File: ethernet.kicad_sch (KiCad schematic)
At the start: 44 parts, among them J5 Bus_RJ45_5-2337992-8, Q12 PJE138K, U10 ULS-12/5-D48N-C, U8 TPS2372-3RGWR, U9 ACPL-217-500E

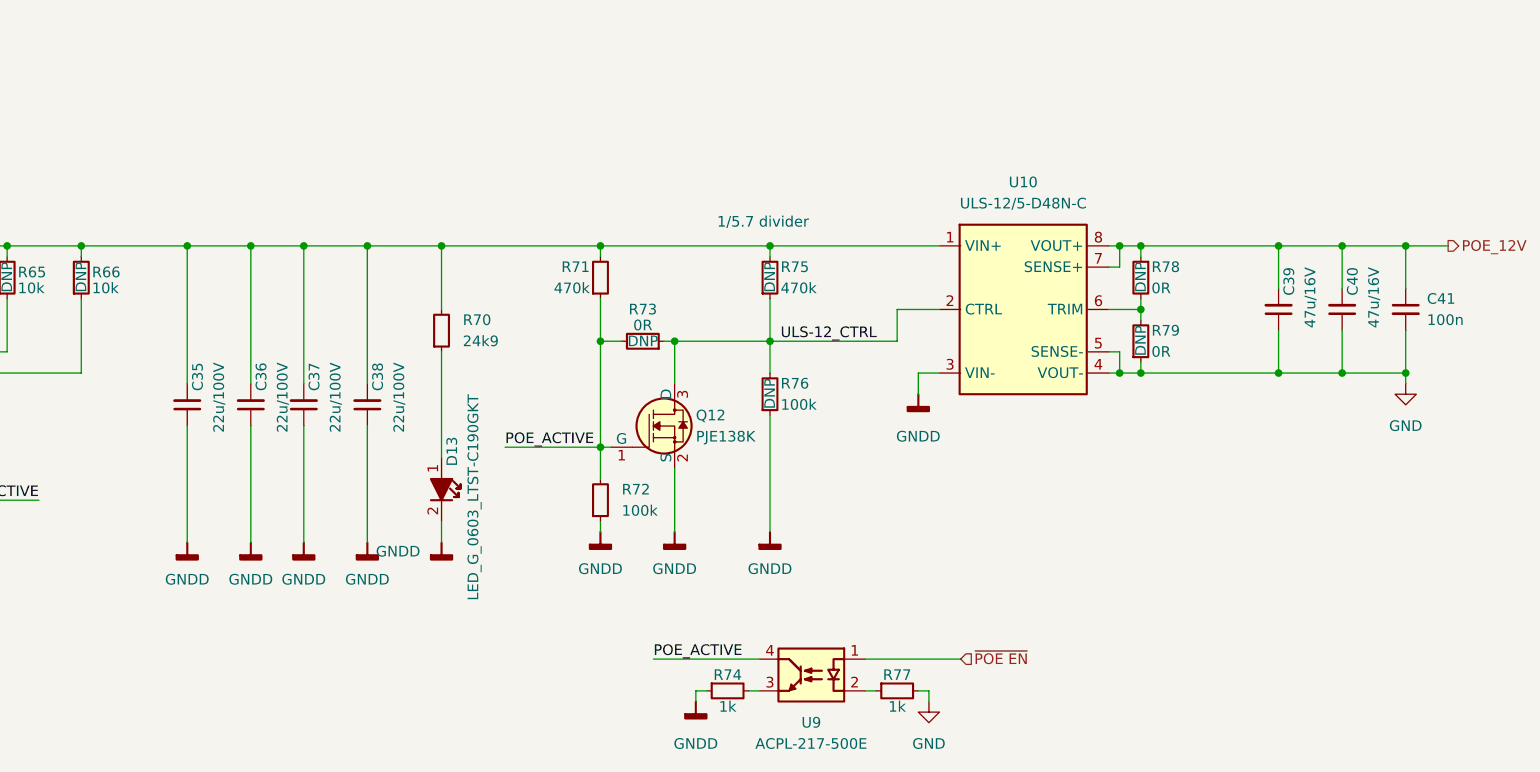
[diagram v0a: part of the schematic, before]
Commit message: [#53805] Change designators orientation in ETH sch
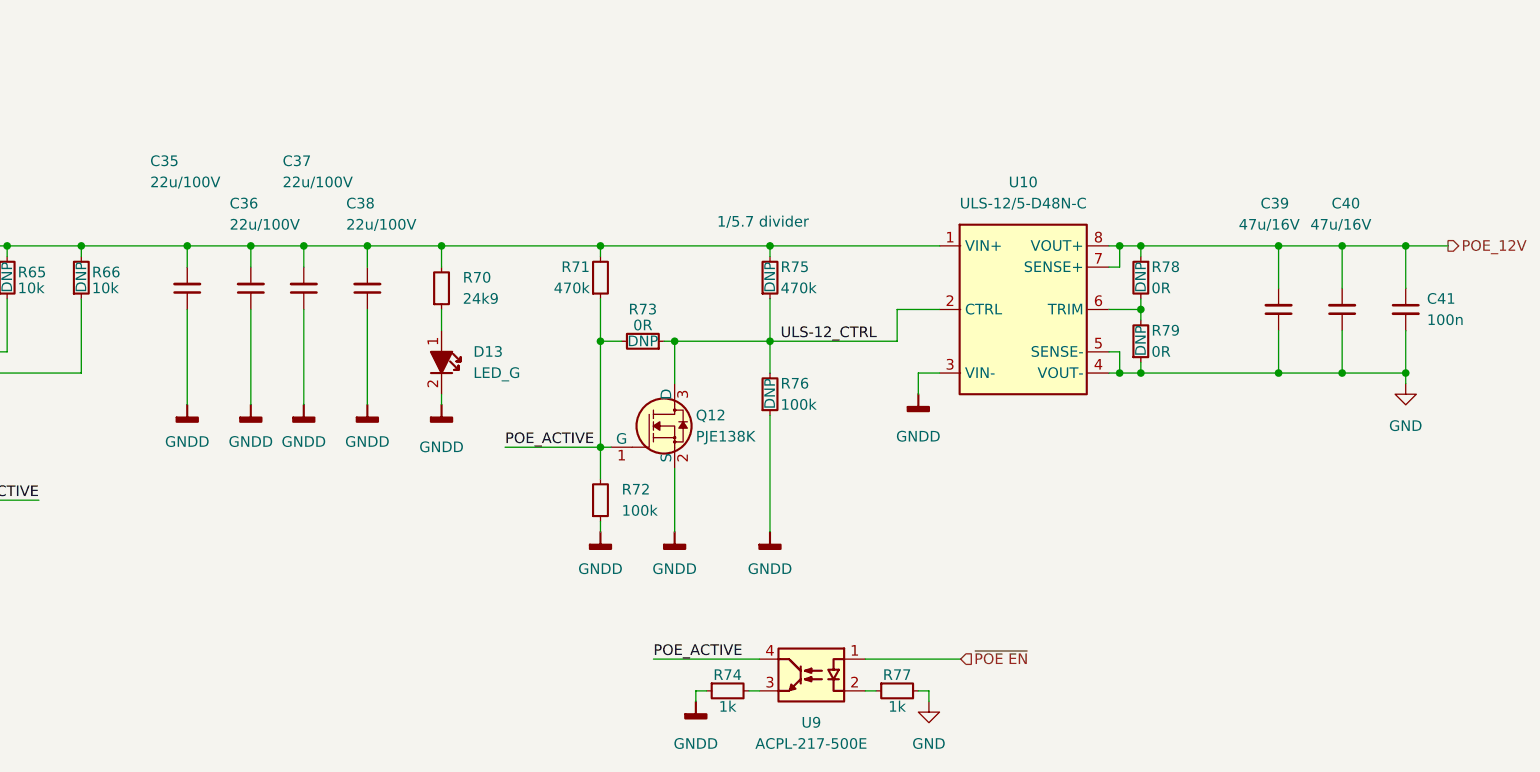
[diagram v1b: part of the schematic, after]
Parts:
- D13: value LED_G_0603_LTST-C190GKT -> LED_G
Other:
- moved on the sheet: C35, C36, C37, C38, D13, R70

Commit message: [#53901] Update capacitor symbols from lib
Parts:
- C32: Dielectric (none) -> X7R; Val 100n/100V -> 100n; Voltage (none) -> 100V
- C35, C36, C37, C38: Dielectric (none) -> X7S; Val 22u/100V -> 22u; Voltage (none) -> 100V
- C39, C40: Dielectric (none) -> X5R; Val 47u/16V -> 47u; Voltage (none) -> 16V
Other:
- moved on the sheet: C35, C36, C37, C38

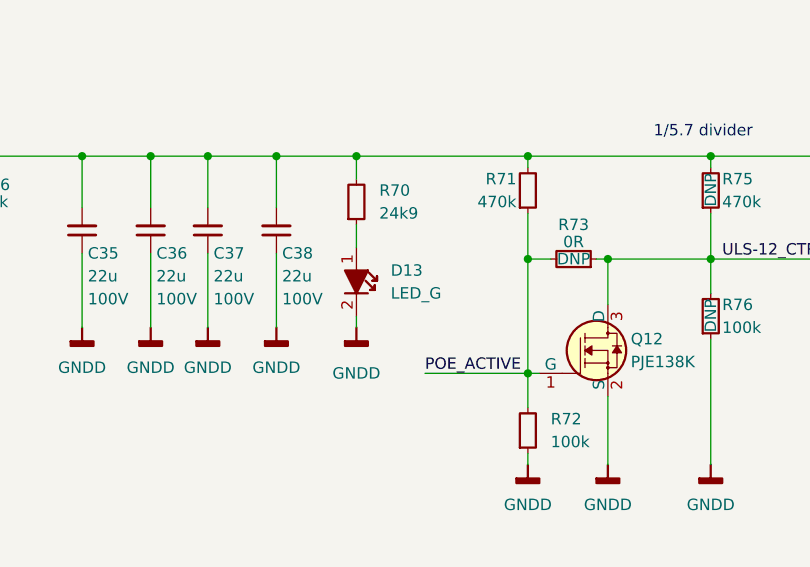
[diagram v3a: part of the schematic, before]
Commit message: [#54617] Uniform diodes MPN
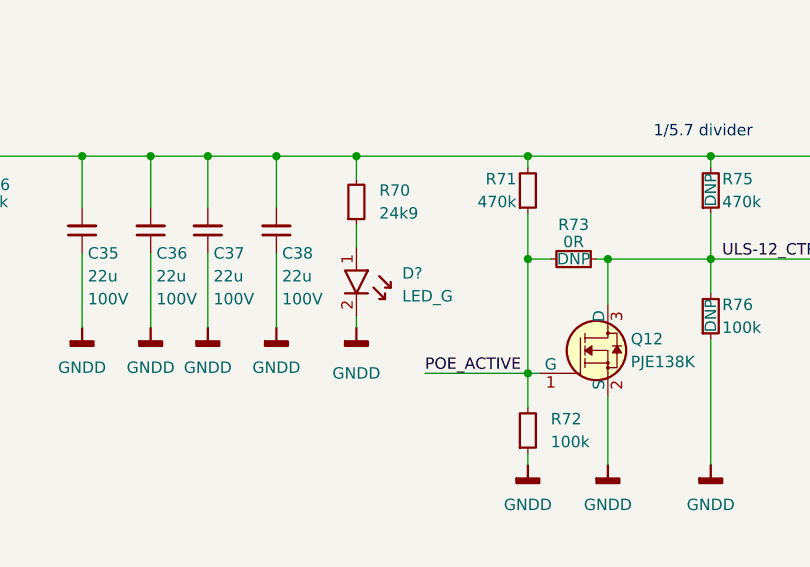
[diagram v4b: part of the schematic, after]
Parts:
- removed D13: LED_G, antmicro-footprints:LED_0603_1608Metric_G, symbol antmicroLEDIndicationDiscrete:LED_G_0603_LTST-C190GKT
- added D?: LED_G, antmicro-footprints:LED_0603_1608Metric_R, symbol antmicroLEDIndicationDiscrete:LED_R_0603_598-8D80-107F
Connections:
- net GNDD: now also D?.2
- net at R70.1: now also D?.1
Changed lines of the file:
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@@
-    (pin "2")
-  )
-  (symbol (lib_id "antmicroLEDIndicationDiscrete:LED_G_0603_LTST-C190GKT") (at 247.65 193.04 270) (unit 1)
-    (in_bom yes) (on_board yes) (fields_autoplaced)
-    (property "Reference" "D13" (id 0) (at 251.46 195.5799 90)
-      (effects (font (size 1.27 1.27)) (justify left))
-    )
-    (property "Value" "LED_G" (id 1) (at 251.46 198.1199 90)
-      (effects (font (size 1.27 1.27) (thickness 0.15)) (justify left))
-    )
-    (property "Footprint" "antmicro-footprints:LED_0603_1608Metric_G" (id 2) (at 237.49 215.9 0)
-      (effects (font (size 1.27 1.27) (thickness 0.15)) (justify left bottom) hide)
-    )
-    (property "Datasheet" "https://media.digikey.com/pdf/Data%20Sheets/Lite-On%20PDFs/LTST-C190GKT.pdf" (id 3) (at 234.95 215.9 0)
-      (effects (font (size 1.27 1.27) (thickness 0.15)) (justify left bottom) hide)
-    )
-    (property "MPN" "LTST-C190GKT" (id 4) (at 232.41 215.9 0)
-      (effects (font (size 1.27 1.27) (thickness 0.15)) (justify left bottom) hide)
-    )
-    (property "Manufacturer" "Lite-On Inc." (id 5) (at 229.87 215.9 0)
-      (effects (font (size 1.27 1.27) (thickness 0.15)) (justify left bottom) hide)
-    )
-    (property "Author" "Antmicro" (id 6) (at 227.33 215.9 0)
-      (effects (font (size 1.27 1.27) (thickness 0.15)) (justify left bottom) hide)
-    )
-    (property "License" "Apache-2.0" (id 7) (at 224.79 215.9 0)
-      (effects (font (size 1.27 1.27) (thickness 0.15)) (justify left bottom) hide)
-    )
-    (pin "1")
     (pin "2")
   )
@@
     (pin "1")
   )
+  (symbol (lib_id "antmicroLEDIndicationDiscrete:LED_R_0603_598-8D80-107F") (at 247.65 193.04 270) (unit 1)
+    (in_bom yes) (on_board yes) (fields_autoplaced)
+    (property "Reference" "D?" (id 0) (at 252.73 195.8974 90)
+      (effects (font (size 1.27 1.27) (thickness 0.15)) (justify left))
+    )
+    (property "Value" "LED_G" (id 1) (at 252.73 198.4374 90)
+      (effects (font (size 1.27 1.27) (thickness 0.15)) (justify left))
+    )
+    (property "Footprint" "antmicro-footprints:LED_0603_1608Metric_R" (id 2) (at 240.03 215.9 0)
+      (effects (font (size 1.27 1.27) (thickness 0.15)) (justify left bottom) hide)
+    )
+    (property "Datasheet" "https://www.farnell.com/datasheets/3093797.pdf" (id 3) (at 237.49 215.9 0)
+      (effects (font (size 1.27 1.27) (thickness 0.15)) (justify left bottom) hide)
+    )
+    (property "MPN" "598-8D80-107F" (id 4) (at 252.73 198.4374 90)
+      (effects (font (size 1.27 1.27) (thickness 0.15)) (justify left) hide)
+    )
+    (property "Manufacturer" "Dialight" (id 5) (at 232.41 215.9 0)
+      (effects (font (size 1.27 1.27) (thickness 0.15)) (justify left bottom) hide)
+    )
+    (property "Author" "Antmicro" (id 6) (at 229.87 215.9 0)
+      (effects (font (size 1.27 1.27) (thickness 0.15)) (justify left bottom) hide)
+    )
+    (property "License" "Apache-2.0" (id 7) (at 227.33 215.9 0)
+      (effects (font (size 1.27 1.27) (thickness 0.15)) (justify left bottom) hide)
+    )
+    (pin "1")
+    (pin "2")
+  )
   (symbol (lib_id "antmicroFerriteBeadsandChips:FB_220Z_2.2A_TDK-MPZ_0603") (at 97.79 213.36 0) (unit 1)

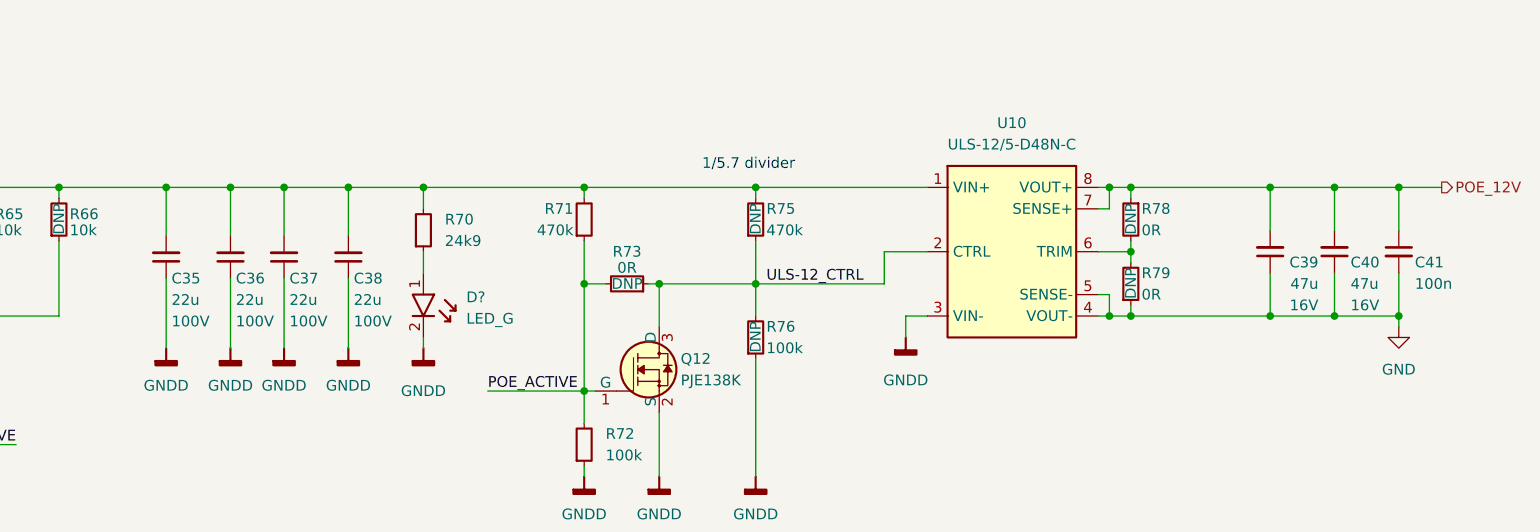
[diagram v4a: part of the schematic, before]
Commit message: [#54617] Reduce capacitors diversity
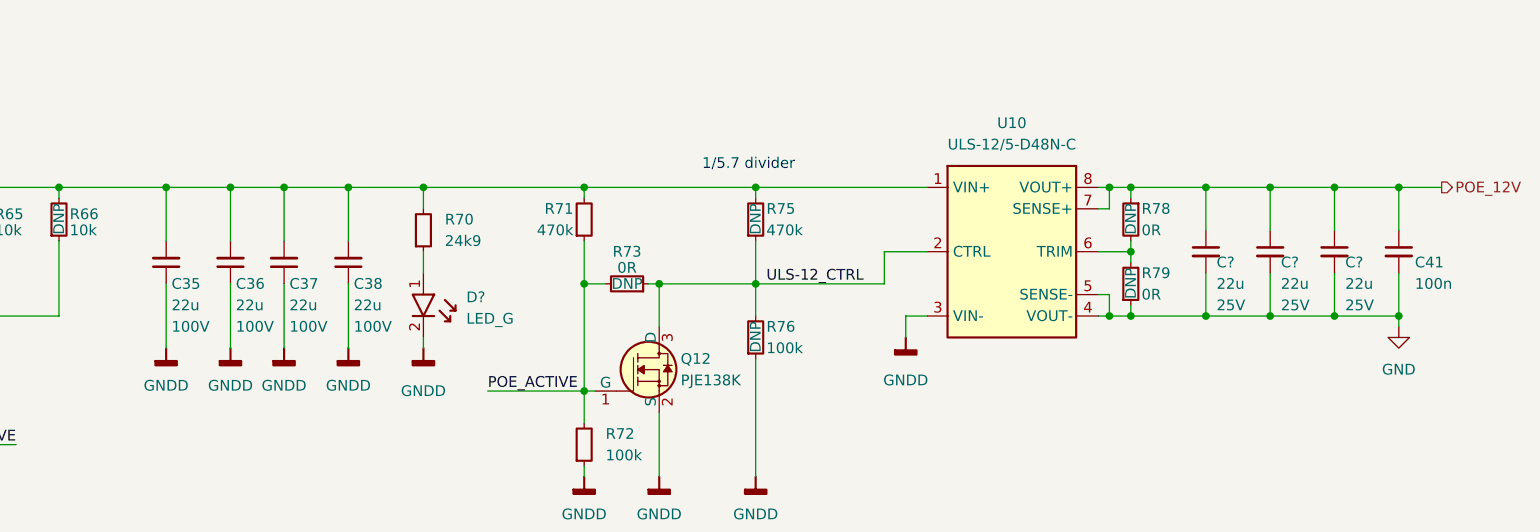
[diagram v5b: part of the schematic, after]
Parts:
- removed C39, C40: C_47u_16V_1206, antmicro-footprints:C_1206_3216Metric, symbol antmicroCapacitorsmisc:C_47u_16V_1206
- added C? (x3): C_22u_25V_0805, antmicro-footprints:C_0805_2012Metric, symbol antmicroCapacitorsmisc:C_22u_25V_0805
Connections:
- net GND: now also C?.2, C?.2, C?.2
- net POE_12V: now also C?.1, C?.1, C?.1
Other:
- moved on the sheet: C35, C36, C37, C38
